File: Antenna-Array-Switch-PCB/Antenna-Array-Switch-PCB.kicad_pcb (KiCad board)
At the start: 4 copper layers, 98 x 98 mm, 195 parts, among them J1001 Conn_Coaxial, J101 Conn_SMA, J102 Conn_SMA, J103 Conn_SMA, J104 Conn_Coaxial, J201 RFShield_OnePiece, J301 Conn_Coaxial, J401 Conn_Coaxial, J501 Conn_Coaxial, J601 Conn_Coaxial, J701 Conn_Coaxial, J801 Conn_Coaxial, J901 Conn_Coaxial, SW201 TS-1187A-B-A-B, SW202 TS-1187A-B-A-B, U1001 TPS22917DBV, U1002 PGA-103, U101 LM1117IMP-3.3, U102 SKY13418-485LF, U201 RP2040-Zero, U301 TPS22917DBV, U302 PGA-103, U401 TPS22917DBV, U402 PGA-103, U501 TPS22917DBV, U502 PGA-103, U601 TPS22917DBV, U602 PGA-103, U701 TPS22917DBV, U702 PGA-103, U801 TPS22917DBV, U802 PGA-103, U901 TPS22917DBV, U902 PGA-103

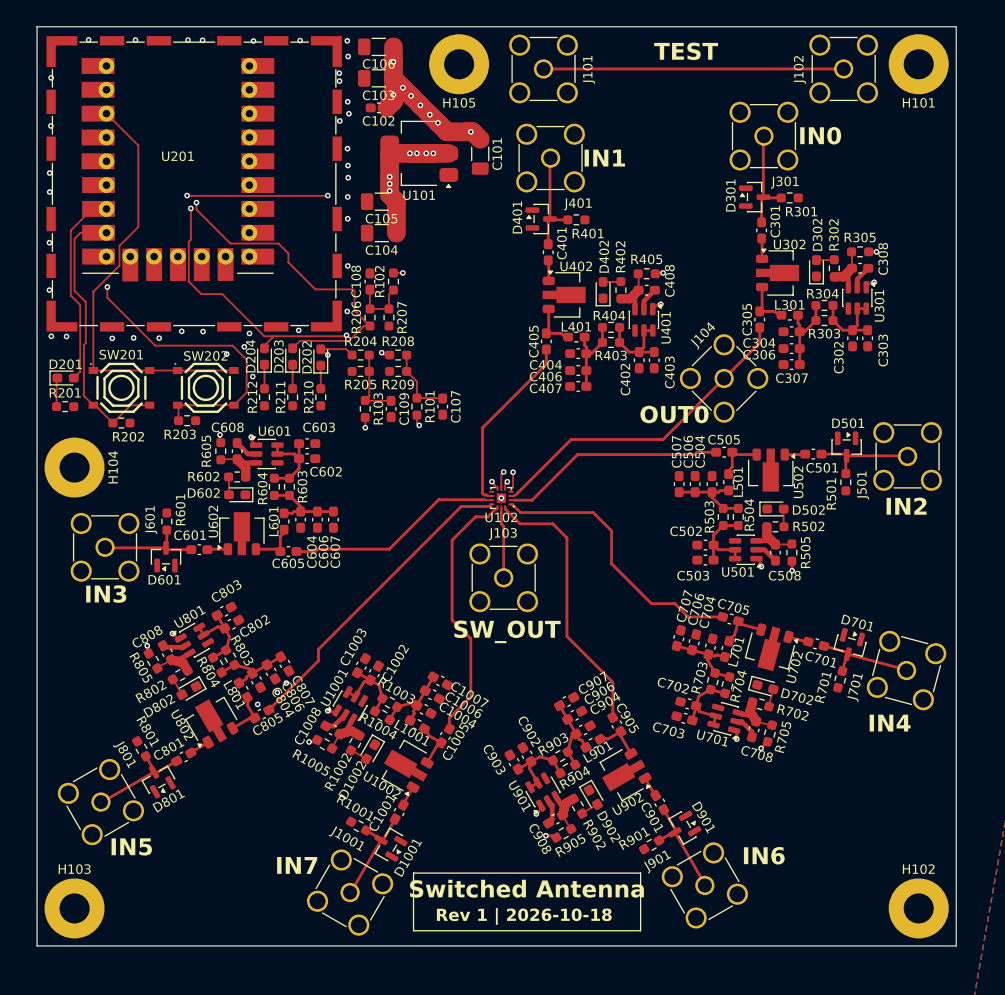
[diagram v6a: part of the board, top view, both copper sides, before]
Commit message: PCB: Add sticking vias and teardrops
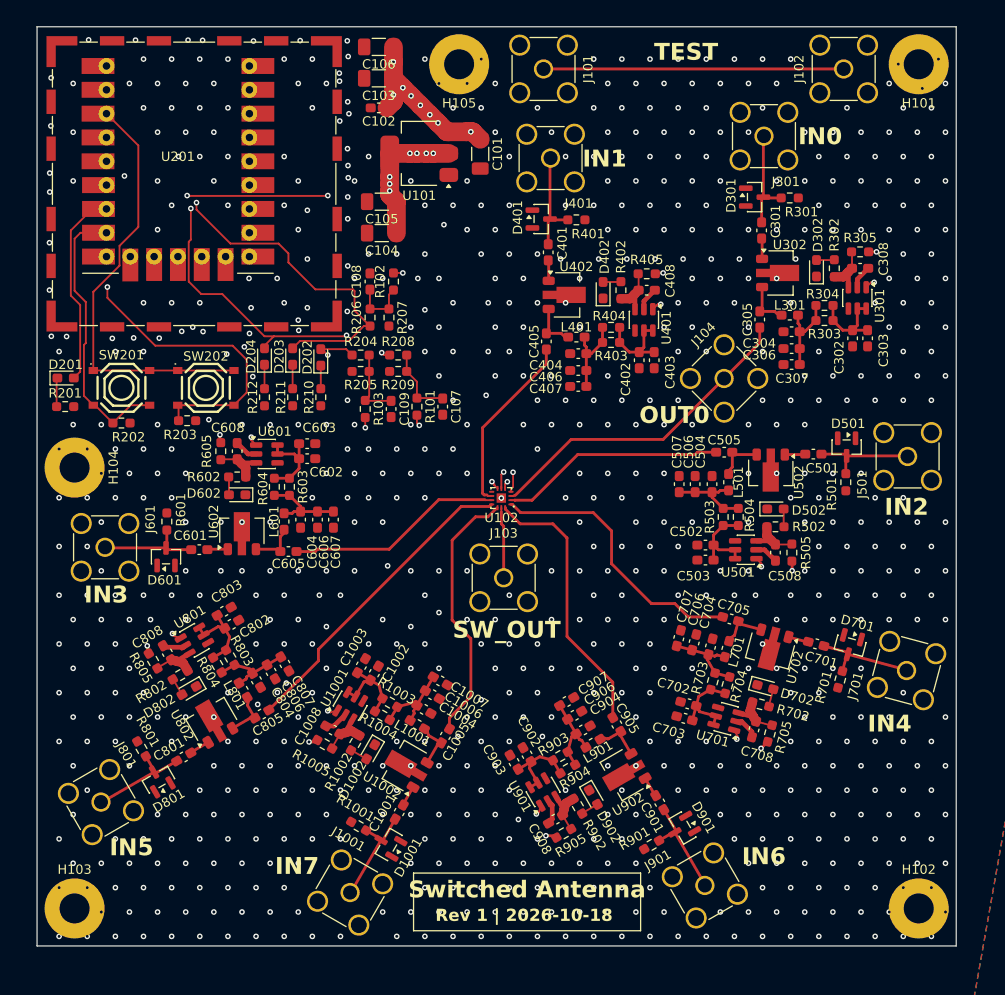
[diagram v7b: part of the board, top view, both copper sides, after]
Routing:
- net GNDA: vias 42 -> 765
